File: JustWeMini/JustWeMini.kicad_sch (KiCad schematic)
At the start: 24 parts, among them J2 Conn_01x02, J3 Conn_01x02, J4 Conn_01x02, J5 Conn_01x02, Q3 -, U10 PCA9557D, U9 AZ1117CR

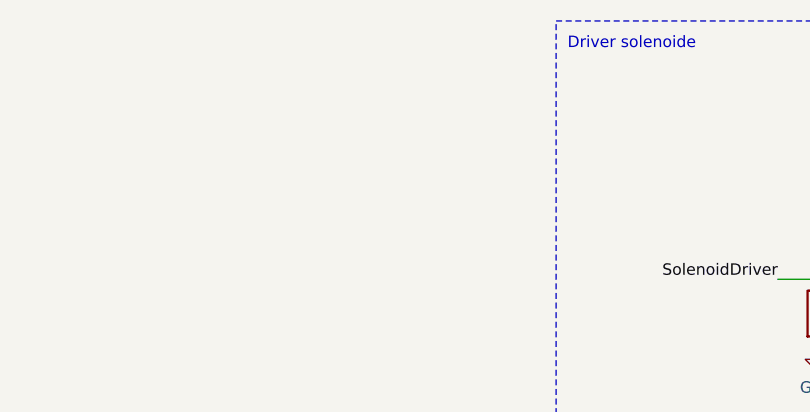
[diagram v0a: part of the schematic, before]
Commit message: Feat: minimal changes, added LED, fixed serigraphy
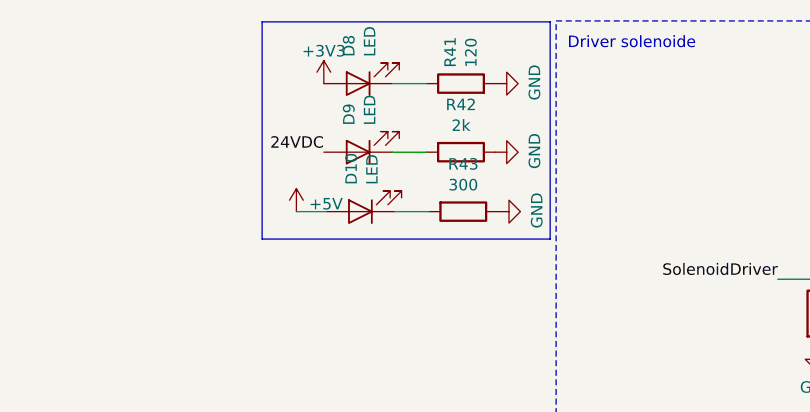
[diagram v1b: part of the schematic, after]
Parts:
- added D10, D8, D9: LED, LED_SMD:LED_0805_2012Metric, symbol Device:LED
- added R41: 120, Resistor_SMD:R_0603_1608Metric, symbol birdchile-rescue:R-device
- added R42: 2k, Resistor_SMD:R_0603_1608Metric, symbol birdchile-rescue:R-device
- added R43: 300, Resistor_SMD:R_0603_1608Metric, symbol birdchile-rescue:R-device
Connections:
- net +3V3: now also D8.2 (A)
- net +5V: now also D10.2 (A)
- net 24VDC: now also D9.2 (A)
- net GND: now also R41.2, R42.1, R43.1
- new net: D10.1 (K), R43.2
- new net: D9.1 (K), R42.2
- new net: D8.1 (K), R41.1

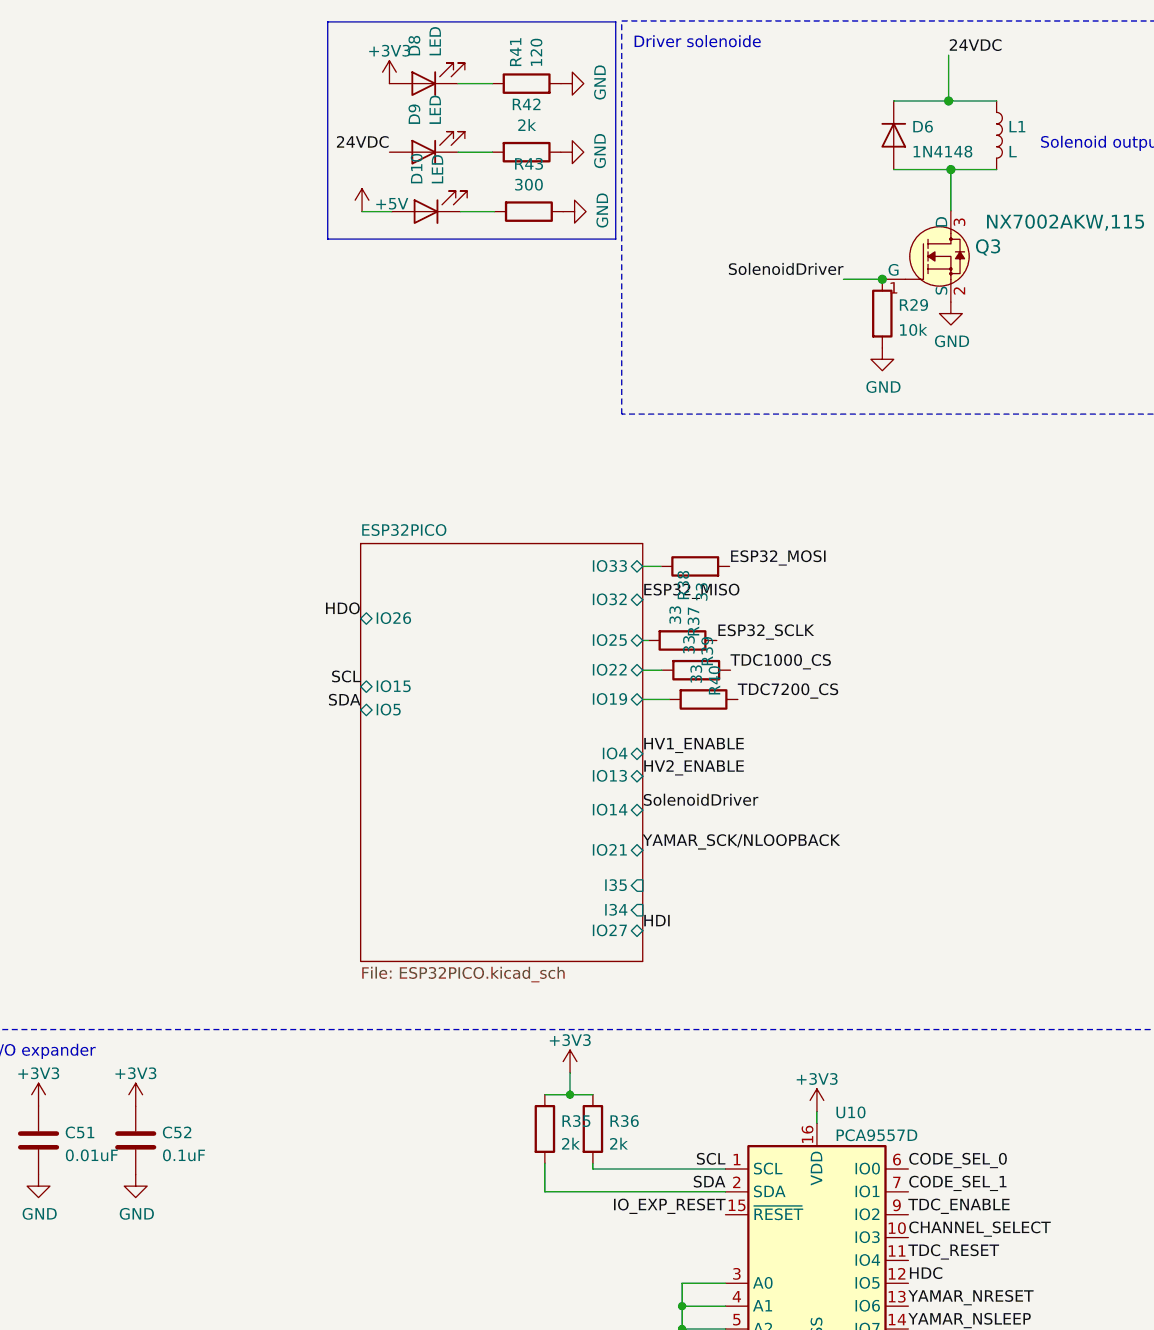
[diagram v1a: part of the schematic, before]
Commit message: Feat: MPN adjusted
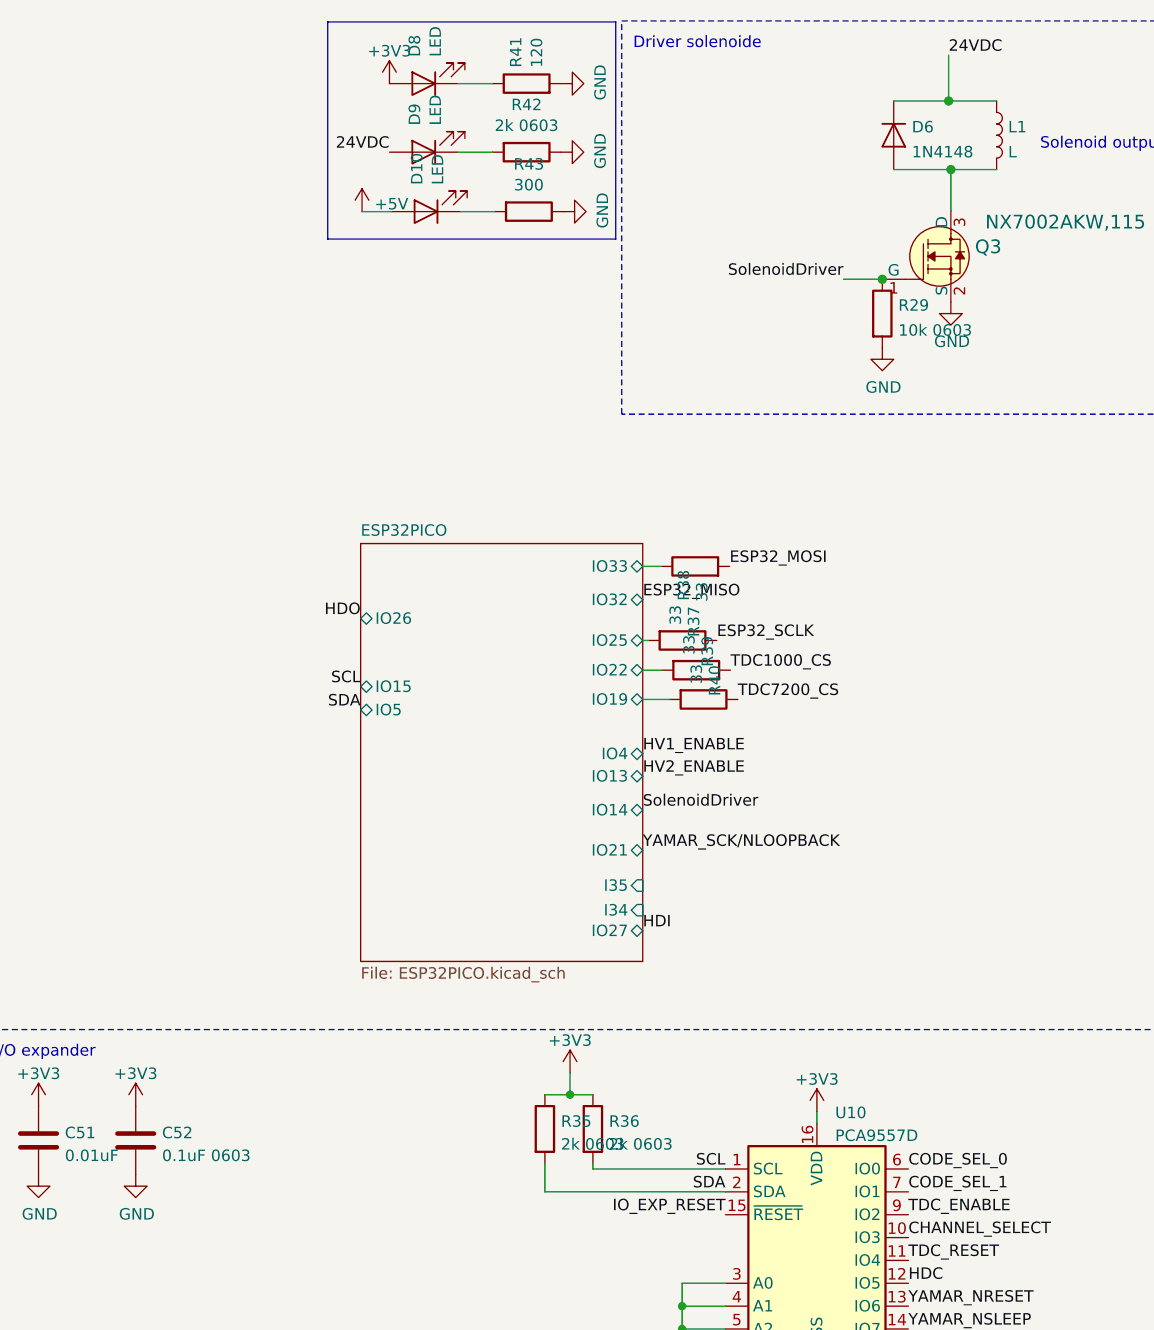
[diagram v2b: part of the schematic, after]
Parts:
- C52: value 0.1uF -> 0.1uF 0603
- R29: value 10k -> 10k 0603
- R35, R36, R42: value 2k -> 2k 0603
